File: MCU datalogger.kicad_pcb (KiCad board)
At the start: 2 copper layers, 51.6 x 32.4 mm, 29 parts, among them J1 Conn_01x04_Pin, J2 Conn_01x04_Pin, J3 Conn_01x09_Pin, J4 Conn_02x03_Odd_Even, U1 24LC1025, U2 24LC1025, U3 DS1337S_, U4 ATMEGA328P-AU, Y1 16 MHz, Y2 32.768 KHz

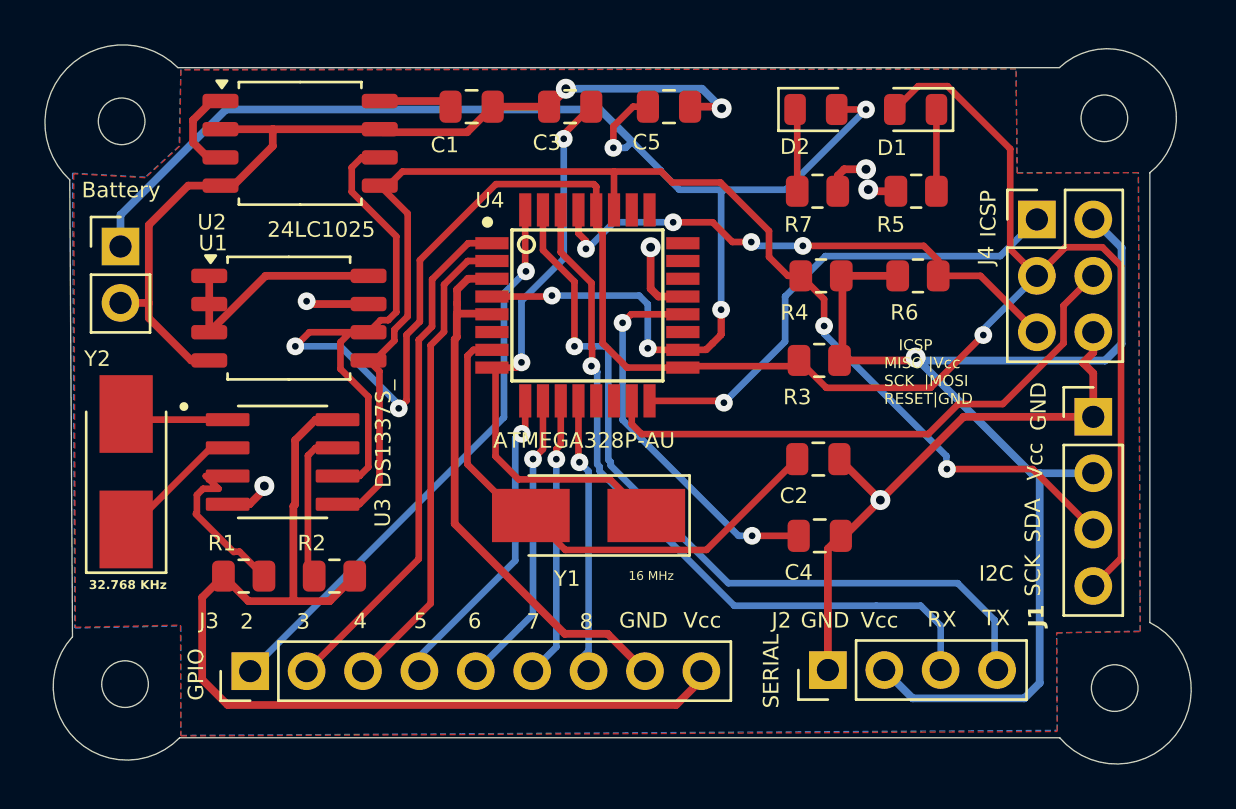
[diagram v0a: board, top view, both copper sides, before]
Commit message: completed 4layer pcb routing
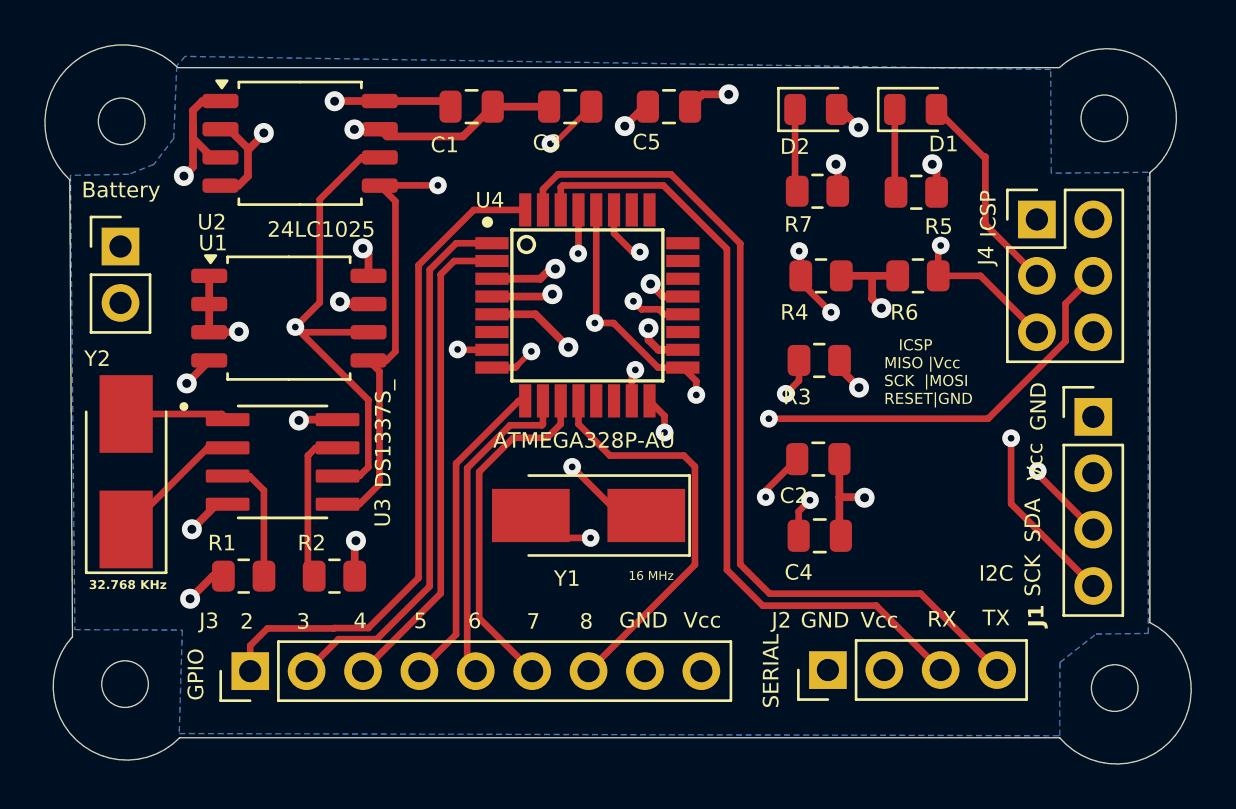
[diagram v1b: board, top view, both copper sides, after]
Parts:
- turned R5 to 180 degrees
- turned D1 to 0 degrees
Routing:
- net /Vcc: track 184.4 -> 36.2 mm, vias 6 -> 13
- net GND: track 105.9 -> 37.6 mm, vias 8 -> 12
- net /SCK: track 108.7 -> 89.5 mm, vias 3 -> 5
- net /D8: track 12.2 -> 18.3 mm, vias 1 -> 0
- net /D2: track 25.8 -> 29.9 mm, vias 1 -> 0
- net Net-(U4-AREF): track 17.3 -> 21.1 mm
- net /TX: track 35.7 -> 39.4 mm, vias 1 -> 0
- net /RX: track 32.8 -> 35.7 mm, vias 1 -> 0
- net /D7: track 12.7 -> 15.6 mm, vias 1 -> 0
- net Net-(U4-PB6): track 24.2 -> 26.6 mm, vias 0 -> 3
- net Net-(U3-~{INTA}): track 7.88 -> 5.76 mm
- net Net-(U4-PB7): track 26.2 -> 24.6 mm, vias 2 -> 3
- net /D6: track 13.4 -> 14.6 mm, vias 1 -> 0
- net /D3: track 23.5 -> 24.7 mm
- net /D4: track 20.9 -> 21.9 mm
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- added copper zone on In2.Cu, net /Vcc
- removed copper zone on F.Cu, net /Vcc
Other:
- copper layers 2 -> 4
